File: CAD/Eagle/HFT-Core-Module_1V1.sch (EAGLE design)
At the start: 401 parts, among them Q0521 ABS07-32.768KHZ, Q0811 ABM03B-32.000MHZ, Q0911 ABM3B-16MHZ-10-R50-1-U, T1201 MMBT2222, T1202 MMBT2222, T1203 MMBT2222, U0111 STM32L4Z_144PIN_SMPS, U0431 PAM2305AAB120, U0601 LM4120IM5-3.0, U0611 MAX5217, U0631 CFPT-141-20MHZ, U0641 OPA354, U0701 Si5338, U0801 SX1276, U0901 AX5243, U0911 PE4259, U0921 PE4259, U0991 PE4259, U1101 MCP3911A0-E-SS, U1111 MAX5136AGTG+, U1121 OPA354, U1131 OPA354, U1141 OPA354, U1201 NHD-C0220BIZ_2X20CHARS, U1301 MPU-9250, U1311 MS5607-02BA03, U1321 SHT31-DIS, U1402 SPV1040T, U1501 TS5A23166, U1601 SC189ZSKTRT, U1701 TS5A23166, U1801 TS5A23166, U1901 TS5A23166, X1261 TTE_EN11-HSM, X1401 WIRE-TO-BOARD_5MM08_1X02, X2001 MOLEX 105017-0001, X2101 SMA_SMT_AMPHENOL-901-143, SAM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, X2111 SMA_SMT_AMPHENOL-901-143, SAM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, X2201 CUI SJ1-3535NS, X2211 CUI SJ1-3535NS, X2311 2X20/90_1MM27_HARWIN_M50-3202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, X2312 2X20/90_1MM27_HARWIN_M50-3202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, X2321 2X20/90_1MM27_HARWIN_M50-3202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, X2322 2X20/90_1MM27_HARWIN_M50-3202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, X2331 2X20/90_1MM27_HARWIN_M50-3202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, X2332 2X20/90_1MM27_HARWIN_M50-3202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

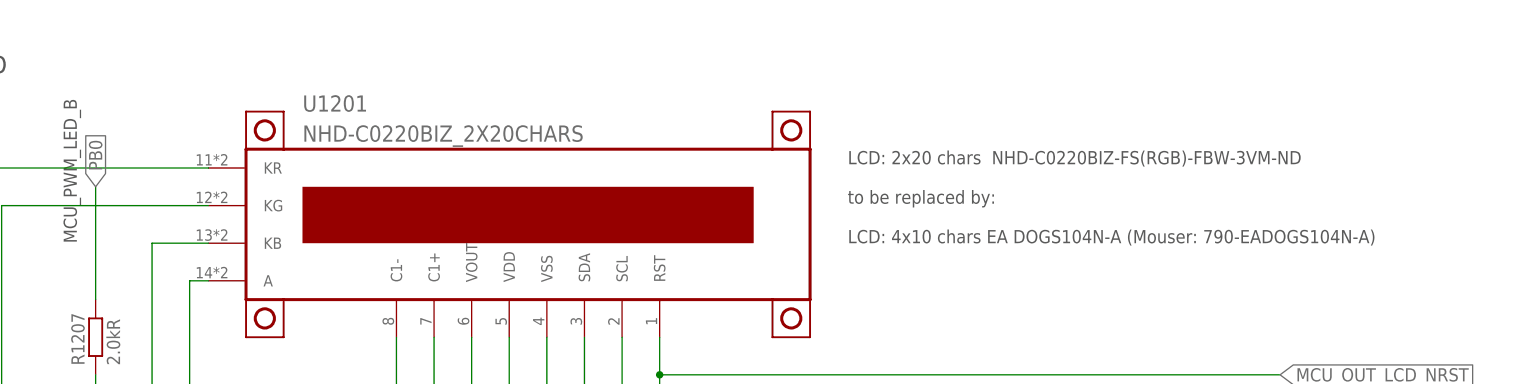
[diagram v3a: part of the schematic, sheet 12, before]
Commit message: HW_1V1 - multiple TODOs for new design added
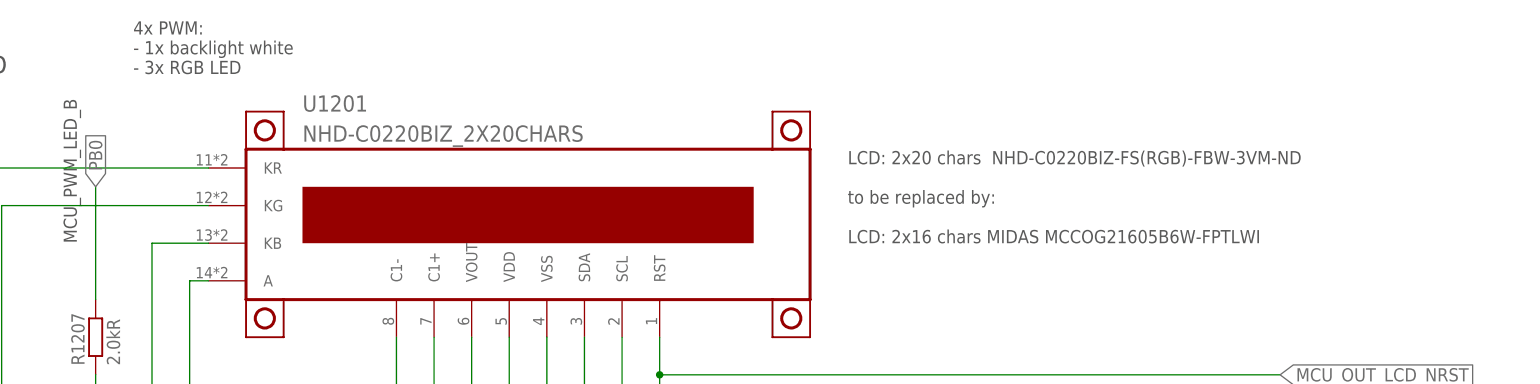
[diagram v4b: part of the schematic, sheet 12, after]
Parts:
- R0638, R0639: value 50R -> 47R
- R0751: value 100R -> N/A
- R1501: value 50R -> 68R
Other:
- note added: "4x PWM: - 1x backlight white - 3x RGB LED"
- note added: "8MHz"
- note added: "LCD: 2x20 chars NHD-C0220BIZ-FS(RGB)-FBW-3VM-ND to be replaced by: LCD: 2x16 chars MIDAS MCCOG21605B6W-FPTLWI"
- note added: "TODO: enable to MCU GPIO out search device w/ lower quiescent current +3V3 to MCU ADC"
- note added: "TODO: enable to MCU-GPIO out +1V2 to MCU-ADC"
- note added: "TODO: fix layout of sockets"
- note added: "to be replaced by: SX1262"
- note removed: "LCD: 2x20 chars NHD-C0220BIZ-FS(RGB)-FBW-3VM-ND to be replaced by: LCD: 4x10 chars EA DOGS104N-A (Mouser: 790-EADOGS104N-A)"
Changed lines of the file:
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@@
 <part name="GND0701" library="df4iah_supply" deviceset="GND" device=""/>
 <part name="GND0702" library="df4iah_supply" deviceset="GND" device=""/>
-<part name="R0751" library="rcl" deviceset="R-EU_" device="R0603" value="100R"/>
+<part name="R0751" library="rcl" deviceset="R-EU_" device="R0603" value="N/A"/>
 <part name="C0715" library="rcl" deviceset="C-EU" device="C0603" value="10nF"/>
 <part name="C0716" library="rcl" deviceset="C-EU" device="C0603" value="10nF"/>
-<part name="R0638" library="rcl" deviceset="R-EU_" device="R0603" value="50R"/>
-<part name="R0639" library="rcl" deviceset="R-EU_" device="R0603" value="50R"/>
+<part name="R0638" library="rcl" deviceset="R-EU_" device="R0603" value="47R"/>
+<part name="R0639" library="rcl" deviceset="R-EU_" device="R0603" value="47R"/>
 <part name="GND0632" library="df4iah_supply" deviceset="GND" device=""/>
 <part name="C0703" library="rcl" deviceset="C-EU" device="C0603" value="100nF"/>
@@
 <part name="R1412" library="rcl" deviceset="R-EU_" device="R0603" value="100kR"/>
 <part name="X1401" library="df4iah_connector" deviceset="WIRE-TO-BOARD_5MM08_1X02" device=""/>
-<part name="R1501" library="df4iah_rcl" deviceset="R-EU_" device="R0805" value="50R"/>
+<part name="R1501" library="df4iah_rcl" deviceset="R-EU_" device="R0805" value="68R"/>
 <part name="R0331" library="rcl" deviceset="R-EU_" device="R0603" value="100kR"/>
 <part name="R0332" library="rcl" deviceset="R-EU_" device="R0603" value="100kR"/>
@@
 <text x="180.34" y="78.74" size="1.778" layer="97">not needed!</text>
 <text x="48.26" y="15.24" size="1.778" layer="97">(1.0A out, 1.5MHz fixed)</text>
+<text x="48.26" y="58.42" size="1.778" layer="97">TODO:
+enable to MCU-GPIO out
++1V2 to MCU-ADC</text>
 </plain>
 <instances>
@@
 <text x="50.8" y="111.76" size="1.778" layer="97">N.C.</text>
 <text x="50.8" y="104.14" size="1.778" layer="97">N.C.</text>
-<text x="50.8" y="96.52" size="1.778" layer="97">10MHz</text>
+<text x="50.8" y="96.52" size="1.778" layer="97"> 8MHz</text>
 <text x="101.6" y="23.622" size="1.778" layer="97" rot="R90">MCU_EXTI7_INTR_SI5338</text>
 <text x="122.936" y="22.098" size="1.778" layer="97" rot="R90">MCU_HSE</text>
@@
 </sheet>
 <sheet>
-<description>VHF/UHF SX1276 - ch 1</description>
+<description>VHF/UHF SX1262 - ch 1</description>
 <plain>
 <text x="22.86" y="162.56" size="2.54" layer="97" ratio="15">VHF / UHF  SX1276 - channel 1
@@
 <text x="241.3" y="43.18" size="1.778" layer="97">NC</text>
 <text x="241.3" y="48.26" size="1.778" layer="97">NC</text>
+<text x="88.9" y="33.02" size="1.778" layer="97">to be replaced by:
+SX1262</text>
 </plain>
 <instances>
@@
 </sheet>
 <sheet>
-<description>VHF/UHF SX1276 - ch 1 - HF sw</description>
+<description>VHF/UHF SX1262 - ch 1 - HF sw</description>
 <plain>
 <text x="50.8" y="25.4" size="1.778" layer="97">HF: high / LF: low</text>
@@
 <text x="160.02" y="139.7" size="1.778" layer="97">LCD: 2x20 chars  NHD-C0220BIZ-FS(RGB)-FBW-3VM-ND
 to be replaced by:
-LCD: 4x10 chars EA DOGS104N-A (Mouser: 790-EADOGS104N-A)</text>
+LCD: 2x16 chars MIDAS MCCOG21605B6W-FPTLWI</text>
 <text x="22.86" y="162.56" size="2.54" layer="97" ratio="15">LC-Display
 I2C addr: 0x3D</text>
@@
 <text x="195.58" y="53.34" size="1.778" layer="97">MCU_IN_RE_Q</text>
 <text x="195.58" y="35.56" size="1.778" layer="97">MCU_IN_RE_PB</text>
+<text x="63.5" y="162.56" size="1.778" layer="97">4x PWM:
+- 1x backlight white
+- 3x RGB LED</text>
 </plain>
 <instances>
@@
 <text x="104.14" y="68.58" size="1.778" layer="97">14mA quiescent current</text>
 <text x="104.14" y="63.5" size="1.778" layer="97">(replaces PAM2305)</text>
+<text x="104.14" y="119.38" size="1.778" layer="97">TODO:
+enable to MCU GPIO out
+search device w/ lower quiescent current
++3V3 to MCU ADC</text>
 </plain>
 <instances>
@@
 <text x="167.64" y="149.86" size="1.778" layer="97">AUDIO IN</text>
 <text x="167.64" y="81.28" size="1.778" layer="97">AUDIO OUT</text>
+<text x="162.56" y="96.52" size="1.778" layer="97">TODO:
+fix layout of sockets</text>
 </plain>
 <instances>

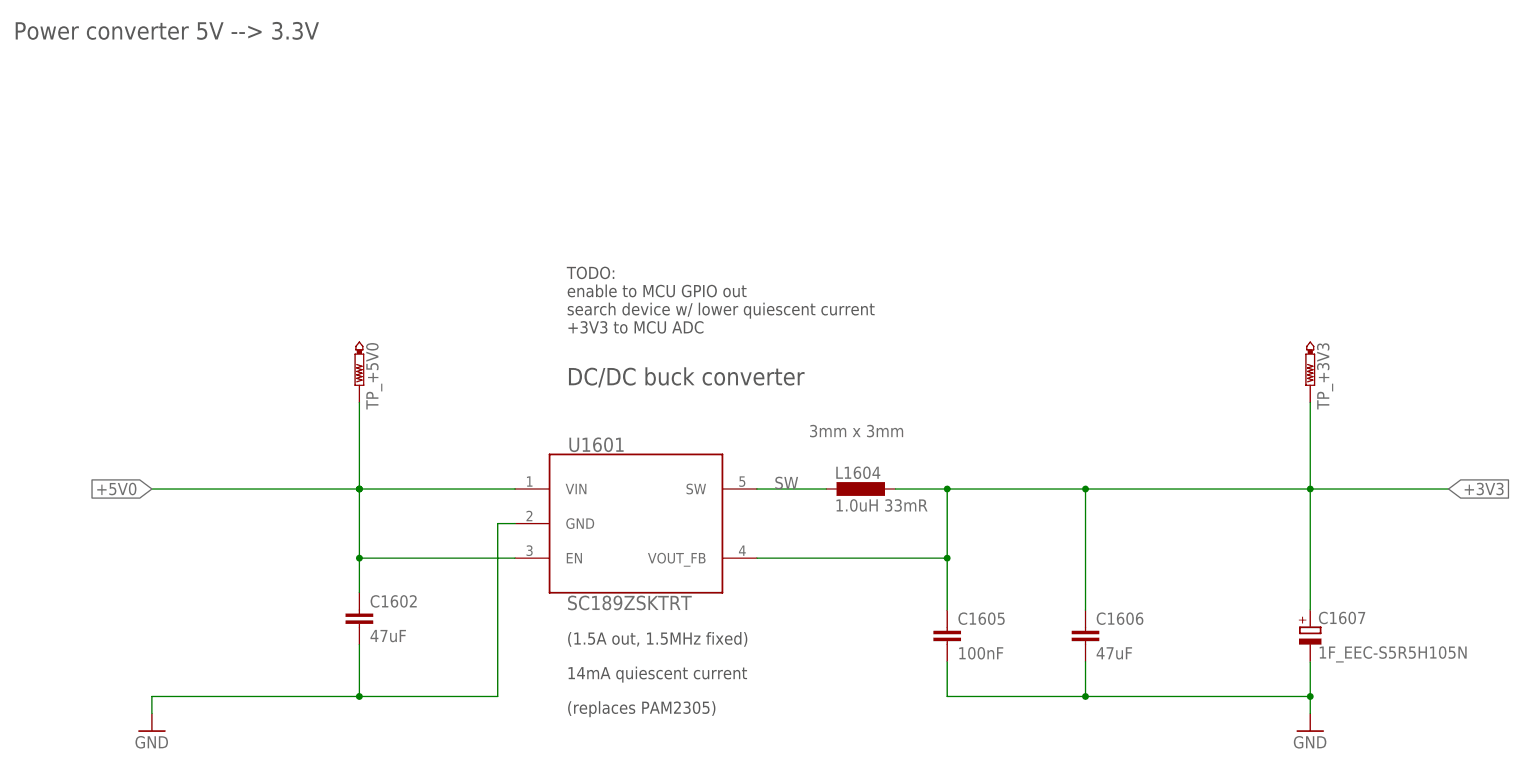
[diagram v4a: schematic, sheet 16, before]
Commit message: HW_1V1 - multiple new modules for V1.1 to be used instead of problematic ones
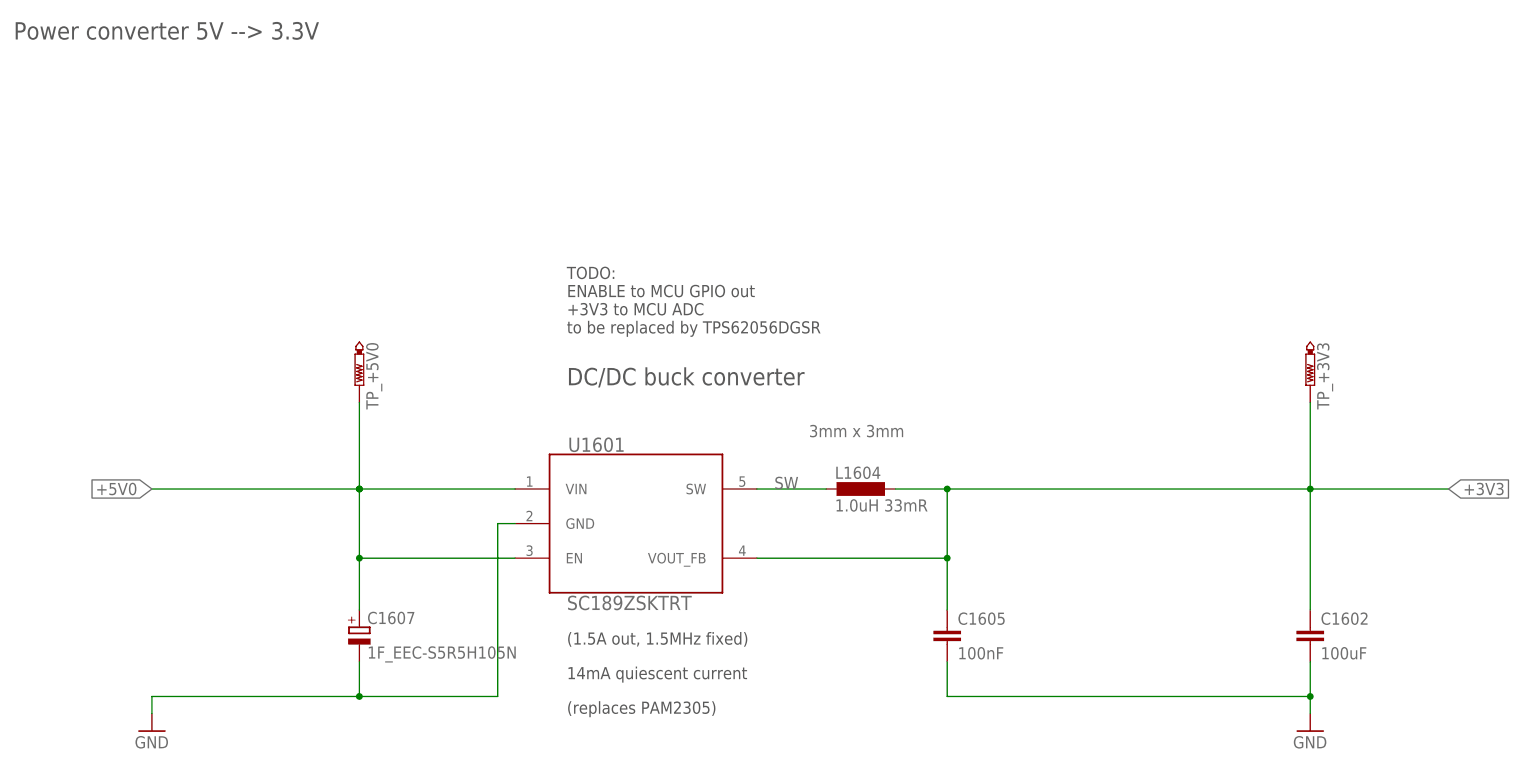
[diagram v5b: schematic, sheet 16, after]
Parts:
- removed C1606: 47uF, rcl:C-EUC0805
- C1401: value 10uF -> 100uF
- C1406: value 47uF -> N/A
- C1602: value 47uF -> 100uF
- R1407: value 100kR -> 120kR
- R1408: value 150kR -> 330kR
- R1501: value 68R -> 100R
- renumbered TP_+3V3_SOL to TP_+5V0_SOL
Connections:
- net +3V3_SOL renamed +5V0_SOL
- net +3V3: now also C1602.1; no longer C1606.1, C1607.+, R1409.2
- net +5V0: now also C1607.+, R1409.2; no longer C1602.1
- net GND: no longer C1606.2
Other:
- note added: "12MHz"
- note added: "LCD-Module I2C addr: 0x3D"
- note added: "TODO: ENABLE to MCU GPIO out +3V3 to MCU ADC to be replaced by TPS62056DGSR"
- note added: "TODO: ENABLE to MCU-GPIO out voltage down (1.05V) to MCU-GPIO out +1V2 to MCU-ADC to be replaced by TPS62051DGSR"
- note added: "Use 10uH, Würth WE-PD 744 777 10"
- note added: "for 3.3V: R1407=100kR, R1408=150kR"
- note added: "for 5.0V: R1407=120kR, R1408=330kR"
- note removed: "8MHz"
- note removed: "LC-Display I2C addr: 0x3D"
- note removed: "TODO: enable to MCU GPIO out search device w/ lower quiescent current +3V3 to MCU ADC"
- note removed: "TODO: enable to MCU-GPIO out +1V2 to MCU-ADC"
- moved on the sheet: C1602, C1607

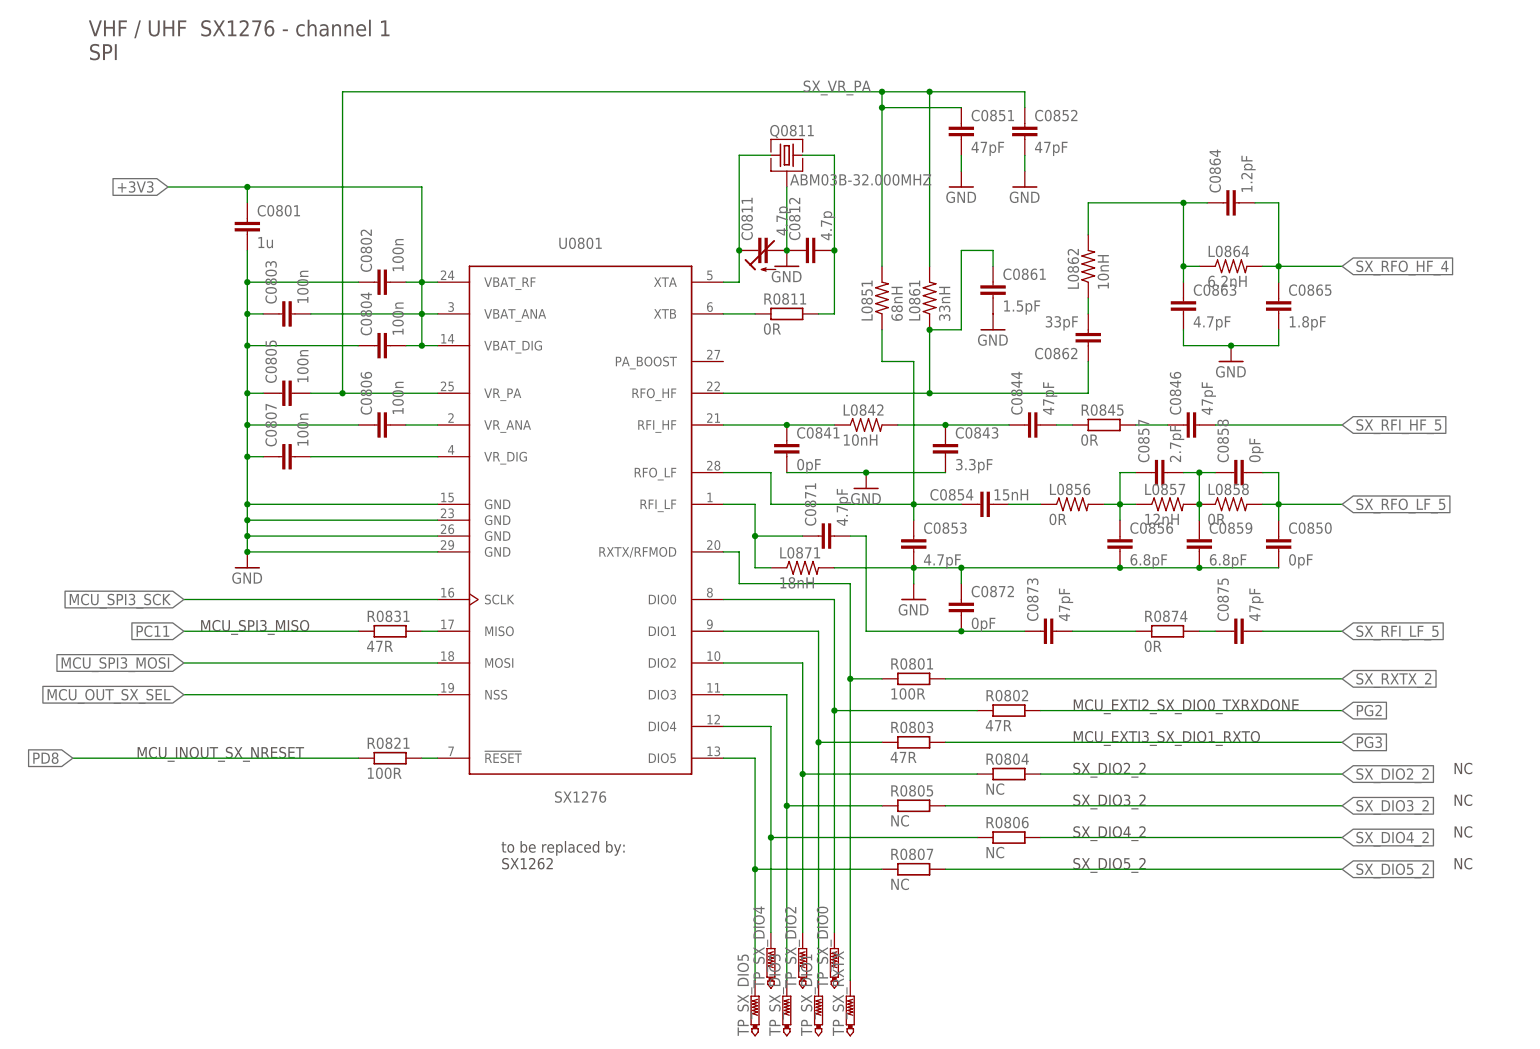
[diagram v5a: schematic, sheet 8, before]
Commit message: HW_1V1 - some values cleaned-up and latest V1.0 issue reminders added
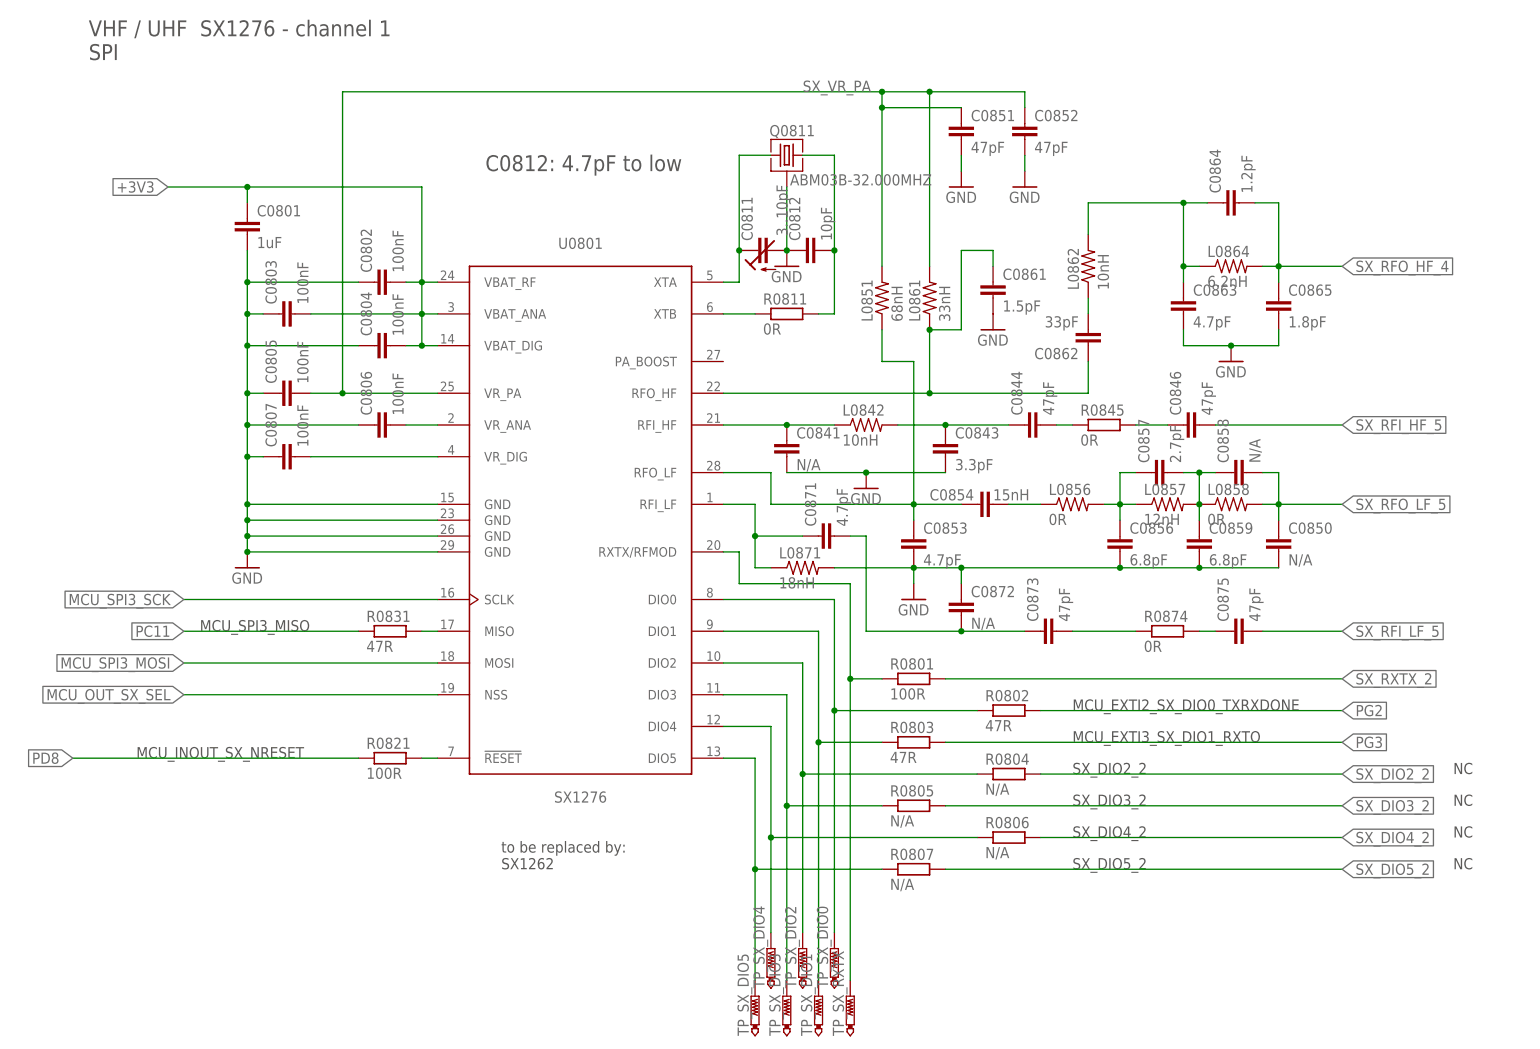
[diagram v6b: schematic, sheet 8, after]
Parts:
- C0401, C0402, C0403, C0404, C0405, C0406, C0407, C0408, C0409, C0802, C0803, C0804, C0805, C0806, C0807: value 100n -> 100nF
- C0801: value 1u -> 1uF
- C0811: value 4.7p -> 3..10pF
- C0812: value 4.7p -> 10pF
- C0841, C0850, C0858, C0872, C_AX_C1, C_AX_C2, C_AX_M2: value 0pF -> N/A
- C0994, C0996: value 0nF HiQ -> N/A HiQ
- C1405: value 0nF -> N/A
- R0611: value open -> N/A
- R0711, R0712: value none -> N/A
- R0804, R0805, R0806, R0807: value NC -> N/A
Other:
- note added: "C0812: 4.7pF to low"
- note added: "D.C."
